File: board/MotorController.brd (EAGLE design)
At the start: 88.9 x 54.6 mm, 41 parts, among them IC1 ATMEGA328P-PU, Q1 BT137-600E, Q2 IPP80P03P4L-04, Q3 SUP75P03-07-H-NH, Y1 16Mhz

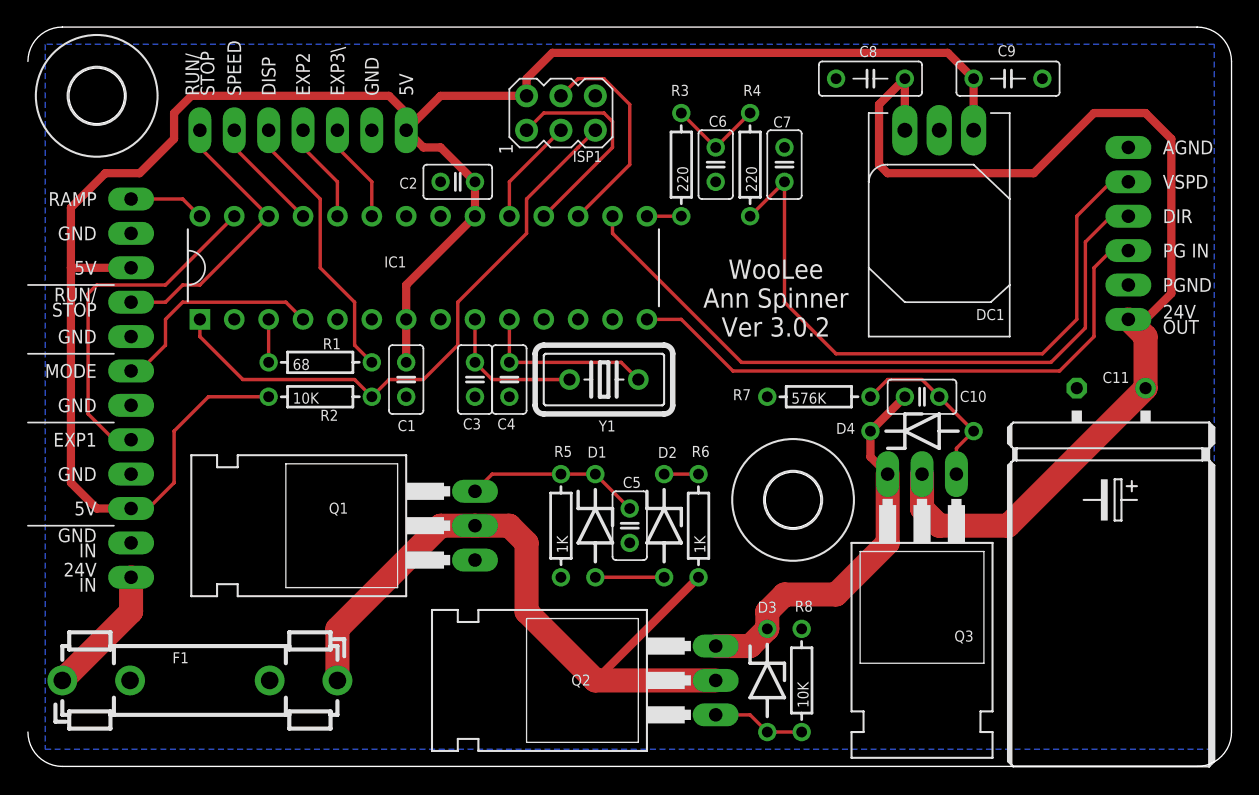
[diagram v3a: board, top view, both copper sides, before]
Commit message: Connect RPM IN to pin 5 which supports interrupts
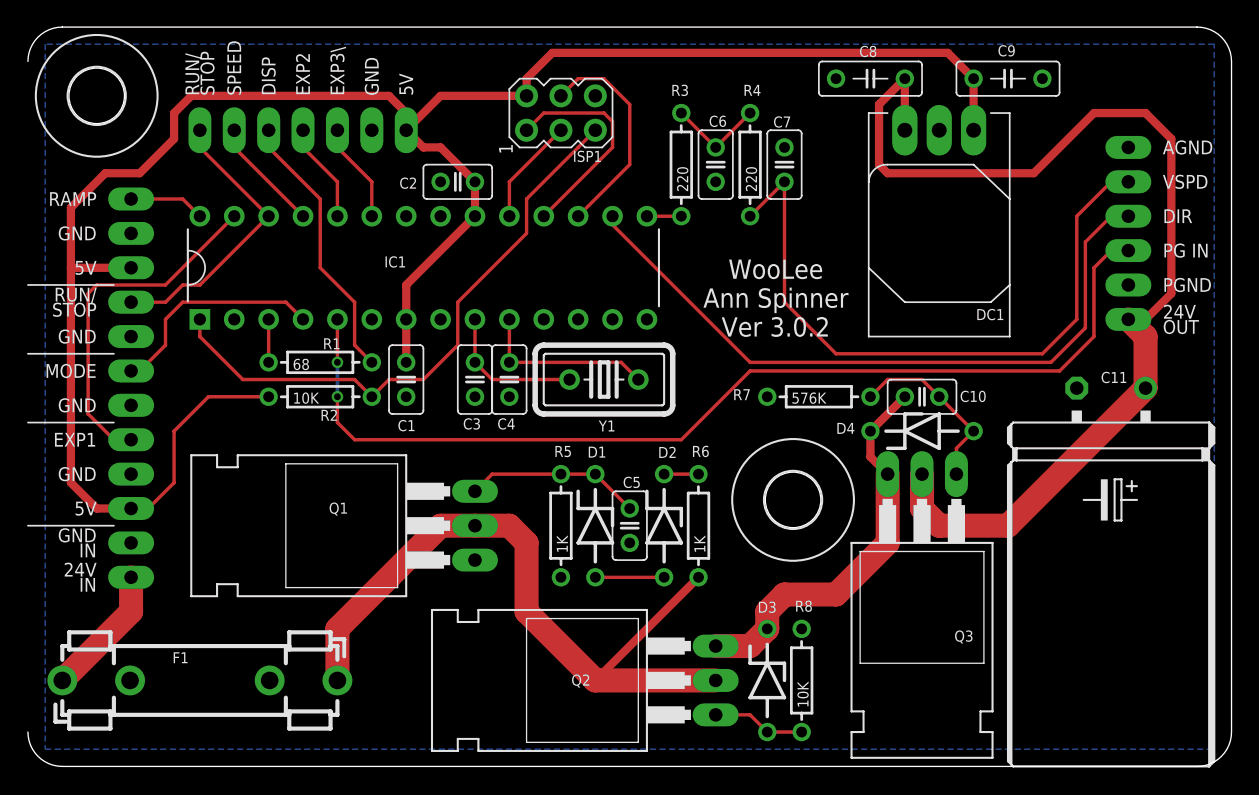
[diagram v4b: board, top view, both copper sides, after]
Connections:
- net RPM_IN: now also IC1.5; no longer IC1.14
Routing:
- net RPM_IN: track 43.8 -> 75.3 mm, vias 0 -> 2
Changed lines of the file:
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@@
 <layer number="113" name="IDFDebug" color="7" fill="1" visible="yes" active="yes"/>
 <layer number="116" name="Patch_BOT" color="9" fill="4" visible="no" active="yes"/>
+<layer number="118" name="Rect_Pads" color="7" fill="1" visible="no" active="no"/>
 <layer number="121" name="_tsilk" color="7" fill="1" visible="yes" active="yes"/>
 <layer number="122" name="_bsilk" color="7" fill="1" visible="no" active="yes"/>
@@
 <layer number="230" name="230bmp" color="7" fill="1" visible="yes" active="yes"/>
 <layer number="231" name="231bmp" color="7" fill="1" visible="yes" active="yes"/>
+<layer number="232" name="Eagle3D_PG2" color="7" fill="1" visible="no" active="no"/>
+<layer number="233" name="Eagle3D_PG3" color="7" fill="1" visible="no" active="no"/>
 <layer number="248" name="Housing" color="7" fill="1" visible="yes" active="yes"/>
 <layer number="249" name="Edge" color="7" fill="1" visible="yes" active="yes"/>
@@
 </element>
 <element name="C11" library="SaintGimp" package="CAP-POL-25-14" value="1000uF" x="80.01" y="10.16" smashed="yes" rot="R270">
-<attribute name="NAME" x="79.375" y="28.321" size="0.8128" layer="25" ratio="10"/>
+<attribute name="NAME" x="79.248" y="28.321" size="0.8128" layer="25" ratio="10"/>
 <attribute name="VALUE" x="76.8858" y="14.9606" size="0.8128" layer="27" ratio="10" rot="R270"/>
 </element>
@@
 <wire x1="66.04" y1="19.05" x2="67.31" y2="17.78" width="1.778" layer="1"/>
 <wire x1="67.31" y1="17.78" x2="72.39" y2="17.78" width="1.778" layer="1"/>
-<wire x1="72.39" y1="17.78" x2="82.55" y2="27.94" width="1.778" layer="1"/>
 <contactref element="24VOUT" pad="1"/>
 <contactref element="C11" pad="+"/>
@@
 <wire x1="82.55" y1="33.02" x2="84.455" y2="34.925" width="0.6096" layer="1"/>
 <wire x1="84.455" y1="34.925" x2="84.455" y2="46.355" width="0.6096" layer="1"/>
-<wire x1="82.55" y1="27.94" x2="82.55" y2="31.75" width="1.778" layer="1"/>
 <wire x1="82.55" y1="31.75" x2="81.28" y2="33.02" width="1.778" layer="1"/>
 <wire x1="63.5" y1="43.815" x2="62.865" y2="44.45" width="0.6096" layer="1"/>
@@
 <wire x1="62.865" y1="48.895" x2="64.77" y2="50.8" width="0.6096" layer="1"/>
 <wire x1="64.77" y1="46.99" x2="64.77" y2="50.8" width="0.6096" layer="1"/>
+<wire x1="82.55" y1="31.75" x2="82.55" y2="27.94" width="1.778" layer="1"/>
+<wire x1="82.55" y1="27.94" x2="72.39" y2="17.78" width="1.778" layer="1"/>
 </signal>
 <signal name="START_IN">
@@
 <signal name="RPM_IN">
 <contactref element="MOTOR" pad="1"/>
-<contactref element="IC1" pad="14"/>
 <wire x1="78.74" y1="36.83" x2="80.01" y2="38.1" width="0.254" layer="1"/>
 <wire x1="80.01" y1="38.1" x2="81.28" y2="38.1" width="0.254" layer="1"/>
 <wire x1="78.74" y1="36.83" x2="78.74" y2="31.75" width="0.254" layer="1"/>
-<wire x1="48.26" y1="33.02" x2="45.72" y2="33.02" width="0.254" layer="1"/>
 <wire x1="78.74" y1="31.75" x2="76.2" y2="29.21" width="0.254" layer="1"/>
-<wire x1="76.2" y1="29.21" x2="52.07" y2="29.21" width="0.254" layer="1"/>
-<wire x1="52.07" y1="29.21" x2="48.26" y2="33.02" width="0.254" layer="1"/>
+<wire x1="76.2" y1="29.21" x2="53.34" y2="29.21" width="0.254" layer="1"/>
+<contactref element="IC1" pad="5"/>
+<wire x1="53.34" y1="29.21" x2="48.26" y2="24.13" width="0.254" layer="1"/>
+<wire x1="48.26" y1="24.13" x2="24.13" y2="24.13" width="0.254" layer="1"/>
+<via x="22.86" y="27.305" extent="1-16" drill="0.5"/>
+<wire x1="22.86" y1="27.305" x2="22.86" y2="29.845" width="0.254" layer="16"/>
+<via x="22.86" y="29.845" extent="1-16" drill="0.5"/>
+<wire x1="22.86" y1="29.845" x2="22.86" y2="33.02" width="0.254" layer="1"/>
+<wire x1="22.86" y1="27.305" x2="22.86" y2="25.4" width="0.254" layer="1"/>
+<wire x1="22.86" y1="25.4" x2="24.13" y2="24.13" width="0.254" layer="1"/>
 </signal>
 <signal name="SPD_OUT">
@@
 <wire x1="80.01" y1="40.64" x2="78.105" y2="38.735" width="0.254" layer="1"/>
 <wire x1="78.105" y1="38.735" x2="78.105" y2="32.385" width="0.254" layer="1"/>
-<wire x1="52.705" y1="29.845" x2="43.18" y2="39.37" width="0.254" layer="1"/>
-<wire x1="43.18" y1="39.37" x2="43.18" y2="40.64" width="0.254" layer="1"/>
 <wire x1="78.105" y1="32.385" x2="75.565" y2="29.845" width="0.254" layer="1"/>
-<wire x1="75.565" y1="29.845" x2="52.705" y2="29.845" width="0.254" layer="1"/>
+<wire x1="75.565" y1="29.845" x2="53.34" y2="29.845" width="0.254" layer="1"/>
+<wire x1="53.34" y1="29.845" x2="43.18" y2="40.005" width="0.254" layer="1"/>
+<wire x1="43.18" y1="40.005" x2="43.18" y2="40.64" width="0.254" layer="1"/>
 </signal>
 <signal name="SPD_IN">
